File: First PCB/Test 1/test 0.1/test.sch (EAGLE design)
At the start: 7 parts, among them SW2 B3U-1000P

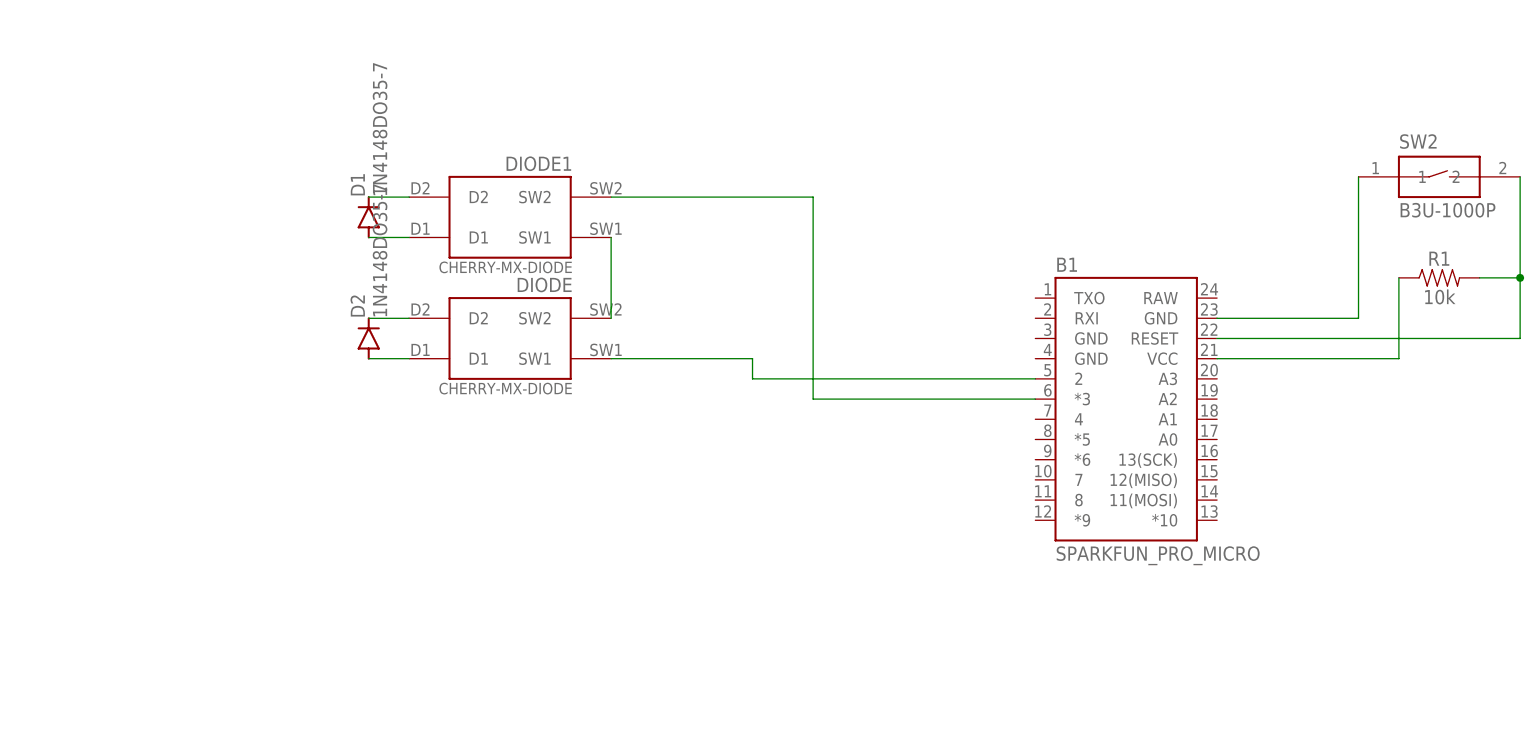
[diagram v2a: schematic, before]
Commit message: slight changes to board layout need to finish still
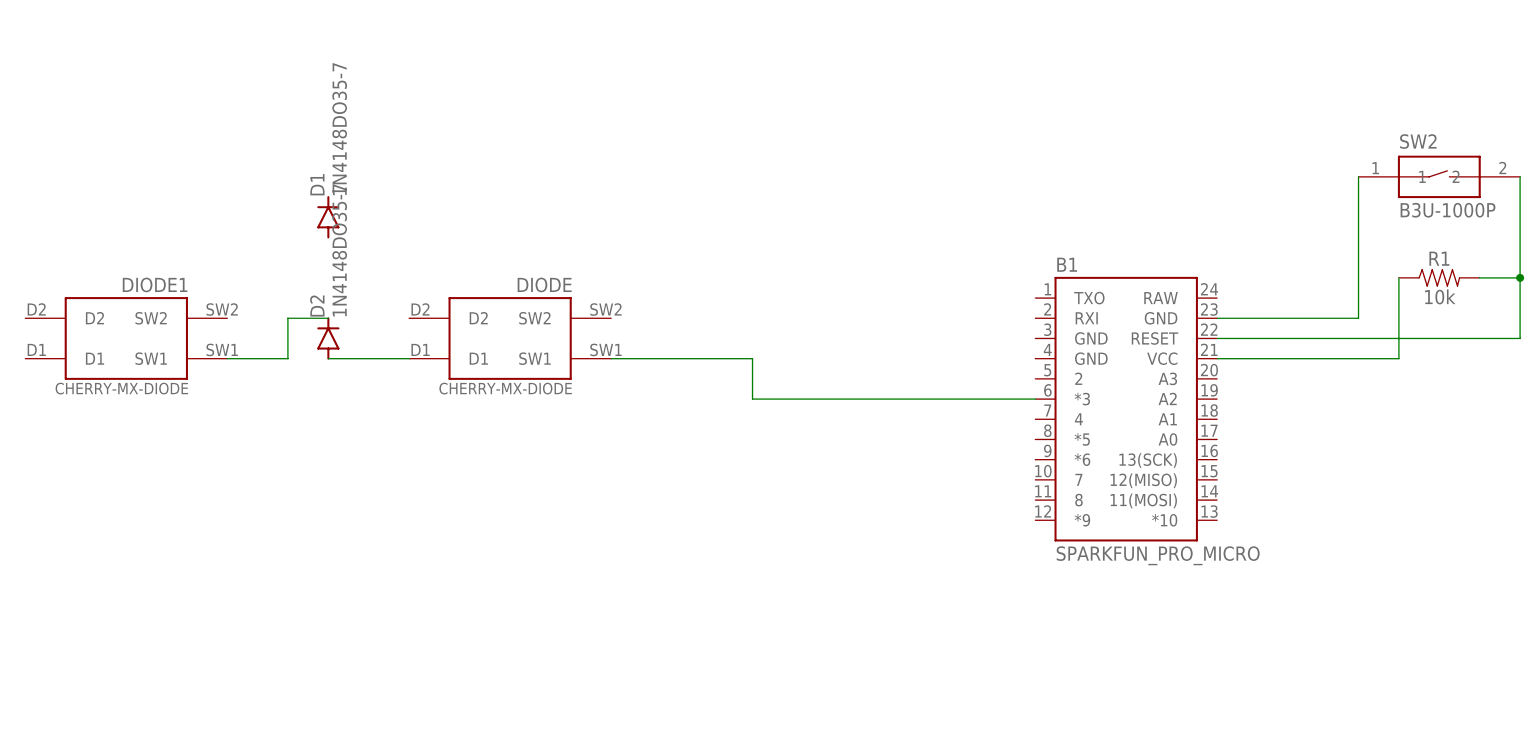
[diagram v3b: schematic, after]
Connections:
- removed net N$10: D1.C, DIODE1.D2
- removed net N$6: B1.*3, DIODE1.SW2
- removed net N$8: D2.C, DIODE.D2
- removed net N$9: D1.A, DIODE1.D1
- net N$4: now also B1.*3; no longer B1.2
- net N$5: now also D2.C; no longer DIODE.SW2
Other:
- moved on the sheet: D1, D2, DIODE1
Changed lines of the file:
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@@
 <attribute name="MPN" x="27.94" y="40.64" size="1.778" layer="96" display="off"/>
 </instance>
-<instance part="D1" gate="G$1" x="7.62" y="55.88" smashed="yes" rot="R90">
-<attribute name="NAME" x="7.1374" y="58.42" size="1.778" layer="95" rot="R90"/>
-<attribute name="VALUE" x="9.9314" y="58.42" size="1.778" layer="96" rot="R90"/>
-<attribute name="OC_NEWARK" x="7.62" y="55.88" size="1.778" layer="96" display="off"/>
-<attribute name="MF" x="7.62" y="55.88" size="1.778" layer="96" display="off"/>
-<attribute name="MPN" x="7.62" y="55.88" size="1.778" layer="96" display="off"/>
+<instance part="D1" gate="G$1" x="2.54" y="55.88" smashed="yes" rot="R90">
+<attribute name="NAME" x="2.0574" y="58.42" size="1.778" layer="95" rot="R90"/>
+<attribute name="VALUE" x="4.8514" y="58.42" size="1.778" layer="96" rot="R90"/>
+<attribute name="OC_NEWARK" x="2.54" y="55.88" size="1.778" layer="96" display="off"/>
+<attribute name="MF" x="2.54" y="55.88" size="1.778" layer="96" display="off"/>
+<attribute name="MPN" x="2.54" y="55.88" size="1.778" layer="96" display="off"/>
 </instance>
-<instance part="DIODE1" gate="G$1" x="27.94" y="55.88" smashed="yes" rot="R180">
-<attribute name="NAME" x="33.274" y="63.5" size="1.778" layer="95" rot="R180"/>
-<attribute name="OC_NEWARK" x="27.94" y="55.88" size="1.778" layer="96" display="off"/>
-<attribute name="MF" x="27.94" y="55.88" size="1.778" layer="96" display="off"/>
-<attribute name="MPN" x="27.94" y="55.88" size="1.778" layer="96" display="off"/>
+<instance part="DIODE1" gate="G$1" x="-20.32" y="40.64" smashed="yes" rot="R180">
+<attribute name="NAME" x="-14.986" y="48.26" size="1.778" layer="95" rot="R180"/>
+<attribute name="OC_NEWARK" x="-20.32" y="40.64" size="1.778" layer="96" display="off"/>
+<attribute name="MF" x="-20.32" y="40.64" size="1.778" layer="96" display="off"/>
+<attribute name="MPN" x="-20.32" y="40.64" size="1.778" layer="96" display="off"/>
 </instance>
-<instance part="D2" gate="G$1" x="7.62" y="40.64" smashed="yes" rot="R90">
-<attribute name="NAME" x="7.1374" y="43.18" size="1.778" layer="95" rot="R90"/>
-<attribute name="VALUE" x="9.9314" y="43.18" size="1.778" layer="96" rot="R90"/>
-<attribute name="OC_NEWARK" x="7.62" y="40.64" size="1.778" layer="96" display="off"/>
-<attribute name="MF" x="7.62" y="40.64" size="1.778" layer="96" display="off"/>
-<attribute name="MPN" x="7.62" y="40.64" size="1.778" layer="96" display="off"/>
+<instance part="D2" gate="G$1" x="2.54" y="40.64" smashed="yes" rot="R90">
+<attribute name="NAME" x="2.0574" y="43.18" size="1.778" layer="95" rot="R90"/>
+<attribute name="VALUE" x="4.8514" y="43.18" size="1.778" layer="96" rot="R90"/>
+<attribute name="OC_NEWARK" x="2.54" y="40.64" size="1.778" layer="96" display="off"/>
+<attribute name="MF" x="2.54" y="40.64" size="1.778" layer="96" display="off"/>
+<attribute name="MPN" x="2.54" y="40.64" size="1.778" layer="96" display="off"/>
 </instance>
 <instance part="SW2" gate="G$1" x="142.24" y="60.96" smashed="yes">
@@
 </segment>
 </net>
-<net name="N$5" class="0">
-<segment>
-<pinref part="DIODE1" gate="G$1" pin="SW1"/>
-<pinref part="DIODE" gate="G$1" pin="SW2"/>
-<wire x1="38.1" y1="43.18" x2="38.1" y2="53.34" width="0.1524" layer="91"/>
-</segment>
-</net>
-<net name="N$6" class="0">
-<segment>
-<pinref part="DIODE1" gate="G$1" pin="SW2"/>
-<wire x1="38.1" y1="58.42" x2="63.5" y2="58.42" width="0.1524" layer="91"/>
-<wire x1="63.5" y1="58.42" x2="63.5" y2="33.02" width="0.1524" layer="91"/>
-<pinref part="B1" gate="G$1" pin="*3"/>
-<wire x1="63.5" y1="33.02" x2="91.44" y2="33.02" width="0.1524" layer="91"/>
-</segment>
-</net>
 <net name="N$4" class="0">
 <segment>
-<pinref part="B1" gate="G$1" pin="2"/>
-<wire x1="91.44" y1="35.56" x2="55.88" y2="35.56" width="0.1524" layer="91"/>
-<wire x1="55.88" y1="35.56" x2="55.88" y2="38.1" width="0.1524" layer="91"/>
 <pinref part="DIODE" gate="G$1" pin="SW1"/>
 <wire x1="55.88" y1="38.1" x2="38.1" y2="38.1" width="0.1524" layer="91"/>
+<pinref part="B1" gate="G$1" pin="*3"/>
+<wire x1="91.44" y1="33.02" x2="55.88" y2="33.02" width="0.1524" layer="91"/>
+<wire x1="55.88" y1="33.02" x2="55.88" y2="38.1" width="0.1524" layer="91"/>
 </segment>
 </net>
@@
 <pinref part="DIODE" gate="G$1" pin="D1"/>
 <pinref part="D2" gate="G$1" pin="A"/>
-<wire x1="12.7" y1="38.1" x2="7.62" y2="38.1" width="0.1524" layer="91"/>
+<wire x1="12.7" y1="38.1" x2="2.54" y2="38.1" width="0.1524" layer="91"/>
 </segment>
 </net>
-<net name="N$8" class="0">
+<net name="N$5" class="0">
 <segment>
 <pinref part="D2" gate="G$1" pin="C"/>
-<pinref part="DIODE" gate="G$1" pin="D2"/>
-<wire x1="7.62" y1="43.18" x2="12.7" y2="43.18" width="0.1524" layer="91"/>
+<wire x1="2.54" y1="43.18" x2="-2.54" y2="43.18" width="0.1524" layer="91"/>
+<wire x1="-2.54" y1="43.18" x2="-2.54" y2="38.1" width="0.1524" layer="91"/>
+<pinref part="DIODE1" gate="G$1" pin="SW1"/>
+<wire x1="-2.54" y1="38.1" x2="-10.16" y2="38.1" width="0.1524" layer="91"/>
 </segment>
 </net>
-<net name="N$9" class="0">
-<segment>
-<pinref part="DIODE1" gate="G$1" pin="D1"/>
-<pinref part="D1" gate="G$1" pin="A"/>
-<wire x1="12.7" y1="53.34" x2="7.62" y2="53.34" width="0.1524" layer="91"/>
-</segment>
-</net>
-<net name="N$10" class="0">
-<segment>
-<pinref part="DIODE1" gate="G$1" pin="D2"/>
-<pinref part="D1" gate="G$1" pin="C"/>
-<wire x1="12.7" y1="58.42" x2="7.62" y2="58.42" width="0.1524" layer="91"/>
-</segment>
-</net>

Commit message: quick file save to match question for geekhack
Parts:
- added U$1, U$2: CHERRY-MX-DIODE, cherrymx:CHERRY-MX-DIODE
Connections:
- removed net N$4: B1.*3, DIODE.SW1
- removed net N$5: D2.C, DIODE1.SW1
- removed net N$7: D2.A, DIODE.D1
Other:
- moved on the sheet: DIODE, DIODE1
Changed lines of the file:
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@@
 <attribute name="OC_NEWARK" value="94X1379"/>
 </part>
+<part name="U$1" library="cherrymx" deviceset="CHERRY-MX-DIODE" device=""/>
+<part name="U$2" library="cherrymx" deviceset="CHERRY-MX-DIODE" device=""/>
 </parts>
 <sheets>
@@
 <attribute name="MPN" x="101.6" y="30.48" size="1.778" layer="96" display="off"/>
 </instance>
-<instance part="DIODE" gate="G$1" x="27.94" y="40.64" smashed="yes" rot="R180">
-<attribute name="NAME" x="33.274" y="48.26" size="1.778" layer="95" rot="R180"/>
-<attribute name="OC_NEWARK" x="27.94" y="40.64" size="1.778" layer="96" display="off"/>
-<attribute name="MF" x="27.94" y="40.64" size="1.778" layer="96" display="off"/>
-<attribute name="MPN" x="27.94" y="40.64" size="1.778" layer="96" display="off"/>
+<instance part="DIODE" gate="G$1" x="25.4" y="33.02" smashed="yes" rot="R270">
+<attribute name="NAME" x="17.78" y="38.354" size="1.778" layer="95" rot="R270"/>
+<attribute name="OC_NEWARK" x="25.4" y="33.02" size="1.778" layer="96" rot="R90" display="off"/>
+<attribute name="MF" x="25.4" y="33.02" size="1.778" layer="96" rot="R90" display="off"/>
+<attribute name="MPN" x="25.4" y="33.02" size="1.778" layer="96" rot="R90" display="off"/>
 </instance>
 <instance part="D1" gate="G$1" x="2.54" y="55.88" smashed="yes" rot="R90">
@@
 <attribute name="MPN" x="2.54" y="55.88" size="1.778" layer="96" display="off"/>
 </instance>
-<instance part="DIODE1" gate="G$1" x="-20.32" y="40.64" smashed="yes" rot="R180">
-<attribute name="NAME" x="-14.986" y="48.26" size="1.778" layer="95" rot="R180"/>
-<attribute name="OC_NEWARK" x="-20.32" y="40.64" size="1.778" layer="96" display="off"/>
-<attribute name="MF" x="-20.32" y="40.64" size="1.778" layer="96" display="off"/>
-<attribute name="MPN" x="-20.32" y="40.64" size="1.778" layer="96" display="off"/>
+<instance part="DIODE1" gate="G$1" x="-22.86" y="30.48" smashed="yes" rot="R270">
+<attribute name="NAME" x="-30.48" y="35.814" size="1.778" layer="95" rot="R270"/>
+<attribute name="OC_NEWARK" x="-22.86" y="30.48" size="1.778" layer="96" rot="R90" display="off"/>
+<attribute name="MF" x="-22.86" y="30.48" size="1.778" layer="96" rot="R90" display="off"/>
+<attribute name="MPN" x="-22.86" y="30.48" size="1.778" layer="96" rot="R90" display="off"/>
 </instance>
 <instance part="D2" gate="G$1" x="2.54" y="40.64" smashed="yes" rot="R90">
@@
 <attribute name="MF" x="142.24" y="48.26" size="1.778" layer="96" display="off"/>
 <attribute name="MPN" x="142.24" y="48.26" size="1.778" layer="96" display="off"/>
+</instance>
+<instance part="U$1" gate="G$1" x="25.4" y="68.58" smashed="yes" rot="R270">
+<attribute name="NAME" x="17.78" y="73.914" size="1.778" layer="95" rot="R270"/>
+</instance>
+<instance part="U$2" gate="G$1" x="-22.86" y="68.58" smashed="yes" rot="R270">
+<attribute name="NAME" x="-30.48" y="73.914" size="1.778" layer="95" rot="R270"/>
 </instance>
 </instances>
@@
 </segment>
 </net>
-<net name="N$4" class="0">
-<segment>
-<pinref part="DIODE" gate="G$1" pin="SW1"/>
-<wire x1="55.88" y1="38.1" x2="38.1" y2="38.1" width="0.1524" layer="91"/>
-<pinref part="B1" gate="G$1" pin="*3"/>
-<wire x1="91.44" y1="33.02" x2="55.88" y2="33.02" width="0.1524" layer="91"/>
-<wire x1="55.88" y1="33.02" x2="55.88" y2="38.1" width="0.1524" layer="91"/>
-</segment>
-</net>
-<net name="N$7" class="0">
-<segment>
-<pinref part="DIODE" gate="G$1" pin="D1"/>
-<pinref part="D2" gate="G$1" pin="A"/>
-<wire x1="12.7" y1="38.1" x2="2.54" y2="38.1" width="0.1524" layer="91"/>
-</segment>
-</net>
-<net name="N$5" class="0">
-<segment>
-<pinref part="D2" gate="G$1" pin="C"/>
-<wire x1="2.54" y1="43.18" x2="-2.54" y2="43.18" width="0.1524" layer="91"/>
-<wire x1="-2.54" y1="43.18" x2="-2.54" y2="38.1" width="0.1524" layer="91"/>
-<pinref part="DIODE1" gate="G$1" pin="SW1"/>
-<wire x1="-2.54" y1="38.1" x2="-10.16" y2="38.1" width="0.1524" layer="91"/>
-</segment>
-</net>

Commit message: finished board and submitted for review, https://geekhack.org/index.php?topic=102077.0
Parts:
- removed DIODE, DIODE1: CHERRY-MX-DIODE, cherrymx:CHERRY-MX-DIODE
- added D3, D4: 1N4148DO35-7, diode:1N4148DO35-7
- added U$3, U$4: CHERRY-MX, cherrymx:CHERRY-MX
- U$1, U$2: value CHERRY-MX-DIODE -> CHERRY-MX; device cherrymx:CHERRY-MX-DIODE -> cherrymx:CHERRY-MX
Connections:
- new net N$10: D4.A, U$2.PIN-2
- new net N$12: D3.A, U$3.PIN-2
- new net N$4: B1.2, D1.C, D2.C
- new net N$5: D1.A, U$1.PIN-2
- new net N$6: B1.4, U$1.PIN-1, U$2.PIN-1
- new net N$7: B1.*3, D3.C, D4.C
- new net N$8: D2.A, U$4.PIN-2
- new net N$9: B1.*5, U$3.PIN-1, U$4.PIN-1
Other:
- moved on the sheet: D1, D2
